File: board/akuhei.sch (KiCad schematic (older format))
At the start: 23 parts, among them J1 CLOCKPORT, J2 I2C, J3 AUXCLK, J4 JTAG, U1 XC9536XL-5VQG44C, U2 PCA9564, U3 TLV70233DBV

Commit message: Finishing touches...
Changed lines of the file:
@@
 EESchema Schematic File Version 2
-LIBS:akuhei-rescue
 LIBS:power
 LIBS:device
@@
 F 0 "J1" H 2300 2400 60  0000 C CNN
 F 1 "CLOCKPORT" H 2300 2150 60  0000 C CNN
-F 2 "con-molex:87758-2216" H 2300 2000 60  0000 C CNN
+F 2 "con-molex:87758-2216" H 2300 2000 60  0001 C CNN
 F 3 "" H 2300 2000 60  0000 C CNN
 	1    2300 2300

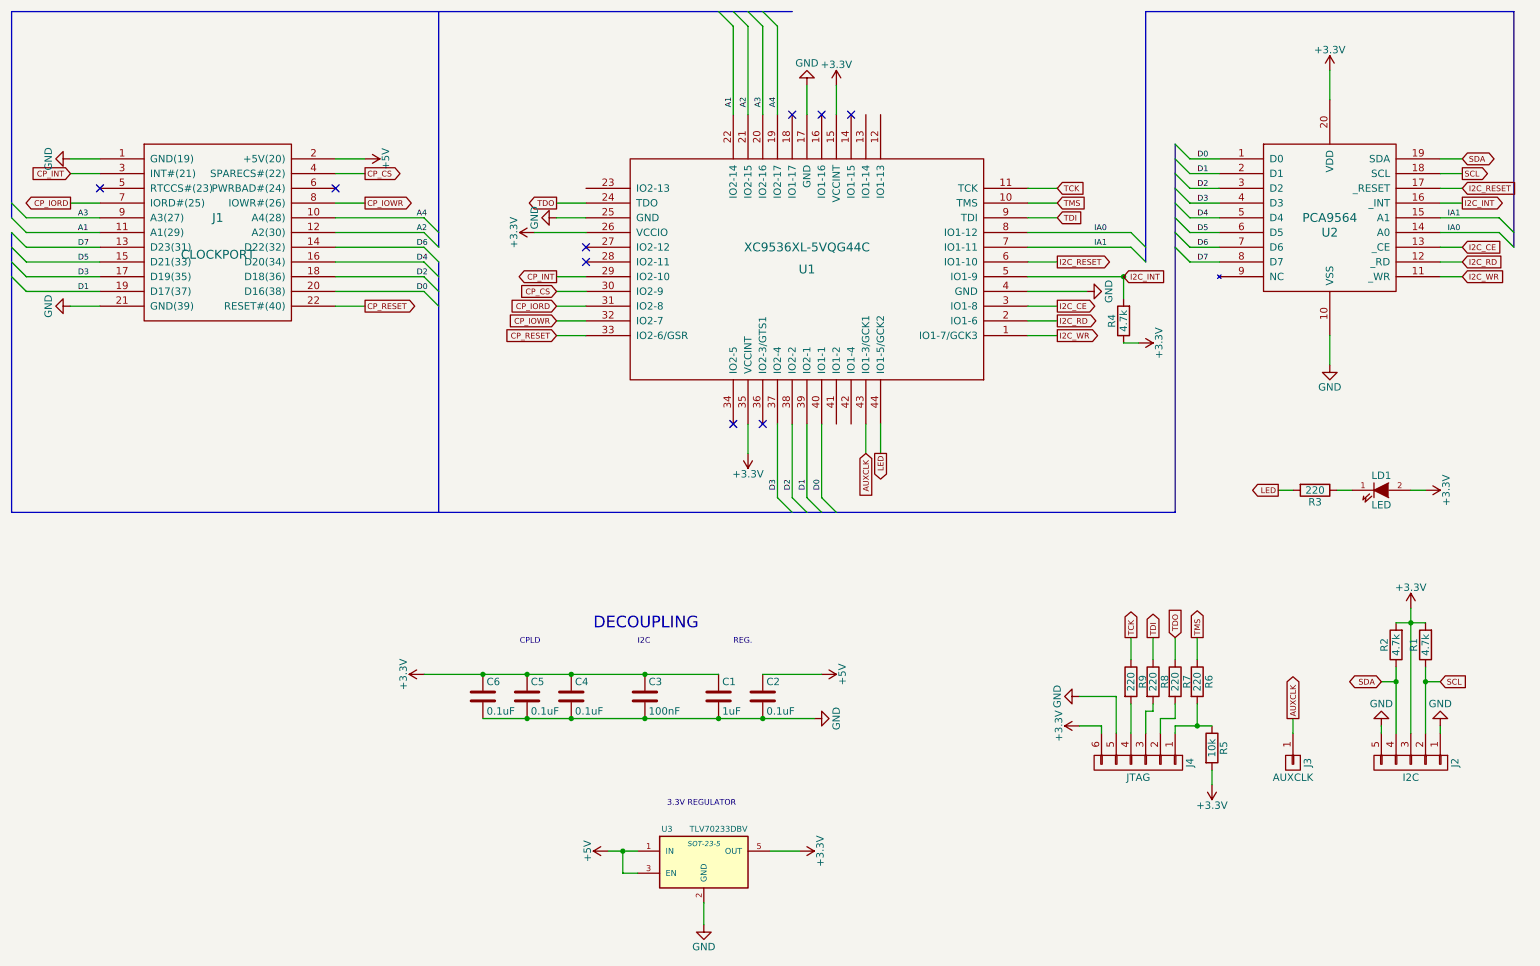
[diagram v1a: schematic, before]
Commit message: Add no-CPLD version.
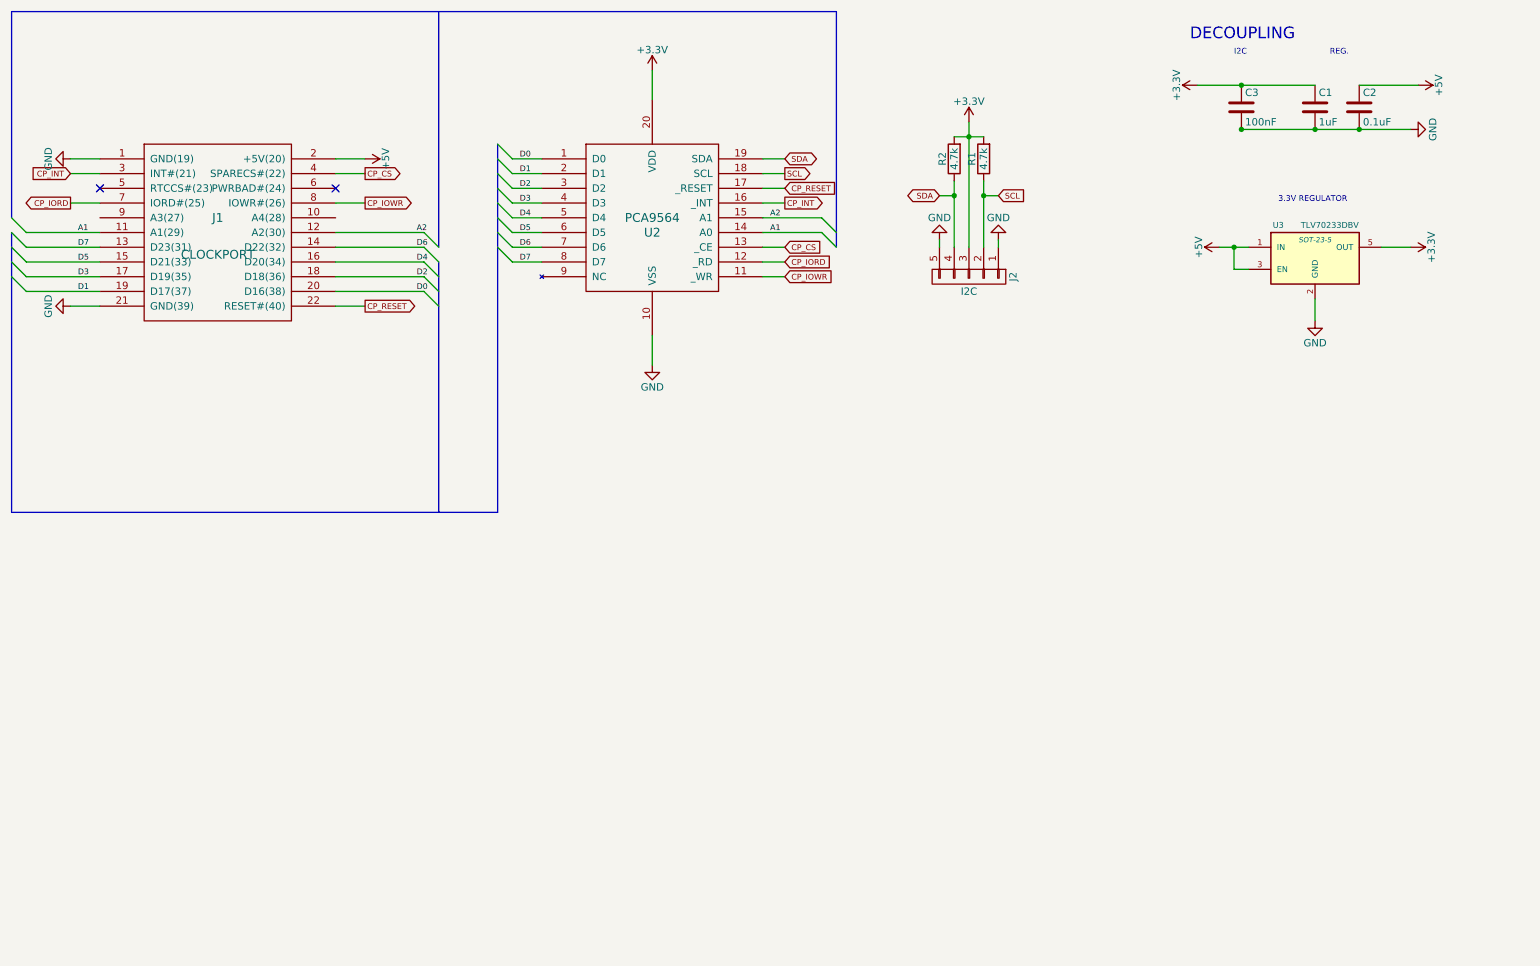
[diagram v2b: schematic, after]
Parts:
- removed C4, C5, C6: 0.1uF, Capacitors_SMD:C_0402, symbol C
- removed J3: AUXCLK, Pin_Headers:Pin_Header_Straight_1x01, symbol CONN_01X01
- removed J4: JTAG, Pin_Headers:Pin_Header_Straight_1x06, symbol CONN_01X06
- removed LD1: LED, LEDs:LED-0603, symbol LED
- removed R3: 220, Resistors_SMD:R_0603, symbol R
- removed R4: 4.7k, Resistors_SMD:R_0603, symbol R
- removed R5: 10k, Resistors_SMD:R_0603, symbol R
- removed R6, R7, R8, R9: 220, Capacitors_SMD:C_0402, symbol R
- removed U1: XC9536XL-5VQG44C, VQFP44, symbol XC9536XL-5VQG44C
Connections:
- net I2C_CE is gone; now on net CP_CS: U2.13 (_CE)
- net I2C_INT is gone; now on net CP_INT: U2.16 (_INT)
- net I2C_RD is gone; now on net CP_IORD: U2.12 (_RD)
- net I2C_RESET is gone; now on net CP_RESET: U2.17 (_RESET)
- net I2C_WR is gone; now on net CP_IOWR: U2.11 (_WR)
- net IA0 is gone; now on net A1: U2.14 (A0)
- net IA1 is gone; now on net A2: U2.15 (A1)
- net A3: no longer names the net of J1.9 (A3(27))
- net A4: no longer names the net of J1.10 (A4(28))
- no-connect marks 9 -> 2
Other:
- note removed: "CPLD"
- moved on the sheet: C1, C2, C3, J2, R1, R2, U2, U3
